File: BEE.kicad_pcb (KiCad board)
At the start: 2 copper layers, 74 x 38 mm, 32 parts, among them J1 RPI1_header, J10 Conn_01x02, J11 Conn_01x02, J12 Conn_01x02, J15 Conn_01x09, J2 Conn_02x05_Odd_Even, J3 Conn_02x03_Odd_Even, J4 Conn_01x06, J5 Conn_02x10_Odd_Even, J6 Conn_01x08, J7 Conn_01x03, J8 Conn_01x08, J9 Conn_01x02, SW1 SW_Push, SW2 SW_Push, SW3 SW_Push, U1 MCP3008, U2 MCP4911

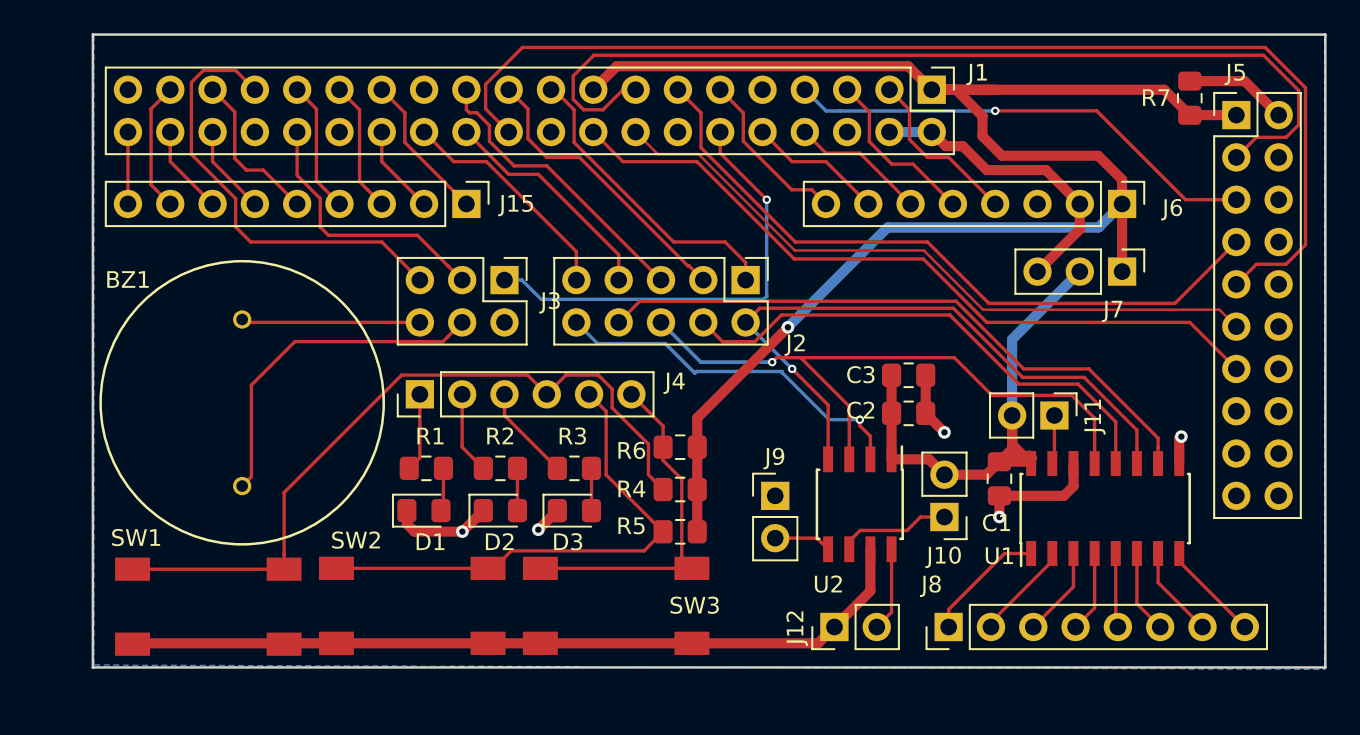
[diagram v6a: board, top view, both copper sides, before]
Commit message: wip: with mounting holes, board a little bit bigger
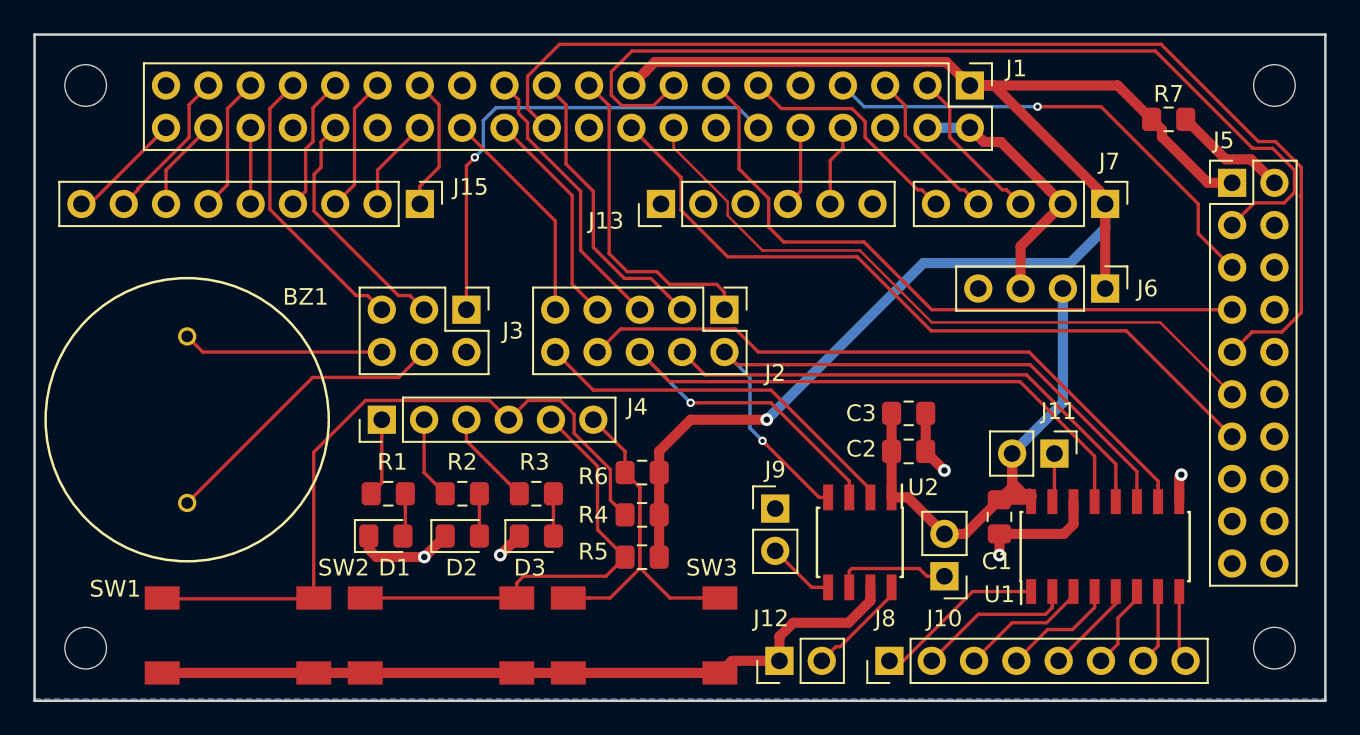
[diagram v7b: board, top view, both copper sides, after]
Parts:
- added H1: MountingHole, MountingHole:MountingHole_2.5mm, F.Cu at (99.6, 83.1)
- added H2: MountingHole, MountingHole:MountingHole_2.5mm, F.Cu at (99.6, 116.8)
- added H3: MountingHole, MountingHole:MountingHole_2.5mm, F.Cu at (170.9, 83.1)
- added H4: MountingHole, MountingHole:MountingHole_2.5mm, F.Cu at (170.9, 116.8)
- added J13: Conn_01x06, Connector_PinHeader_2.54mm:PinHeader_1x06_P2.54mm_Vertical, F.Cu at (134.1, 90.2)
- J6: value Conn_01x08 -> Conn_01x04; footprint Connector_PinHeader_2.54mm:PinHeader_1x08_P2.54mm_Vertical -> Connector_PinHeader_2.54mm:PinHeader_1x04_P2.54mm_Vertical
- J7: value Conn_01x03 -> Conn_01x05; footprint Connector_PinHeader_2.54mm:PinHeader_1x03_P2.54mm_Vertical -> Connector_PinHeader_2.54mm:PinHeader_1x05_P2.54mm_Vertical
- moved J6 5.18 mm to (160.8, 95.2)
- moved J7 4.19 mm to (160.8, 90.2)
- moved J8 4.10 mm to (147.8, 117.6)
- moved J5 4.07 mm to (168.4, 88.9)
- moved J12 3.88 mm to (141.2, 117.6)
- moved J10 3.56 mm to (151.1, 112.5)
- moved BZ1 3.45 mm to (105.7, 103.1)
- moved J3 2.90 mm to (122.4, 96.5)
- moved J15 2.79 mm to (119.6, 90.2)
- moved D1 2.75 mm to (117.6, 110.1)
- moved J4 2.75 mm to (117.3, 103.1)
- moved R1 2.75 mm to (117.7, 107.6)
- moved R4 2.75 mm to (133.0, 108.8)
- moved R5 2.75 mm to (133.0, 111.4)
- moved R6 2.75 mm to (133.0, 106.3)
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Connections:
- J15 pad 5: /BCM19 -> /BCM16
- J15 pad 6: /BCM16 -> /BCM19
- J5 pad 15: Net-(J5-Pad15) -> (no net)
- J5 pad 17: Net-(J5-Pad17) -> (no net)
- J5 pad 19: Net-(J5-Pad19) -> (no net)
- J6 pad 2: +5V -> VDD
- J6 pad 3: GND -> +5V
- J6 pad 4: /BCM2_SDA -> GND
- J7 pad 2: VDD -> +5V
- J7 pad 3: +5V -> /BCM2_SDA
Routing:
- net /SCLK: track 38.7 -> 49.4 mm
- net /BCM13_PWM1: track 26.7 -> 17.2 mm
- net +3V3: track 102.0 -> 96.5 mm
- net /SW1: track 21.1 -> 25.5 mm
- net /BCM17: track 10.2 -> 14.2 mm
- net Net-(J8-Pad2): track 6.89 -> 10.5 mm
- net /SW2: track 30.6 -> 27.2 mm
- net /BCM14_TX: track 8.14 -> 4.89 mm
- net /BCM15_RX: track 8.14 -> 4.89 mm
- net Net-(J8-Pad1): track 8.35 -> 11.2 mm
- net /BCM21: track 4.32 -> 6.97 mm
- net Net-(BZ1-Pad1): track 20.5 -> 18.0 mm
- net Net-(J8-Pad3): track 6.04 -> 8.47 mm
- net +5V: track 18.3 -> 16.2 mm
- net Net-(J8-Pad4): track 5.34 -> 7.43 mm
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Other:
- board size 74 x 38 mm -> 77.5 x 40 mm

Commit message: uart connector with jumpers to select crossed or direct connection. rerouted and labeled
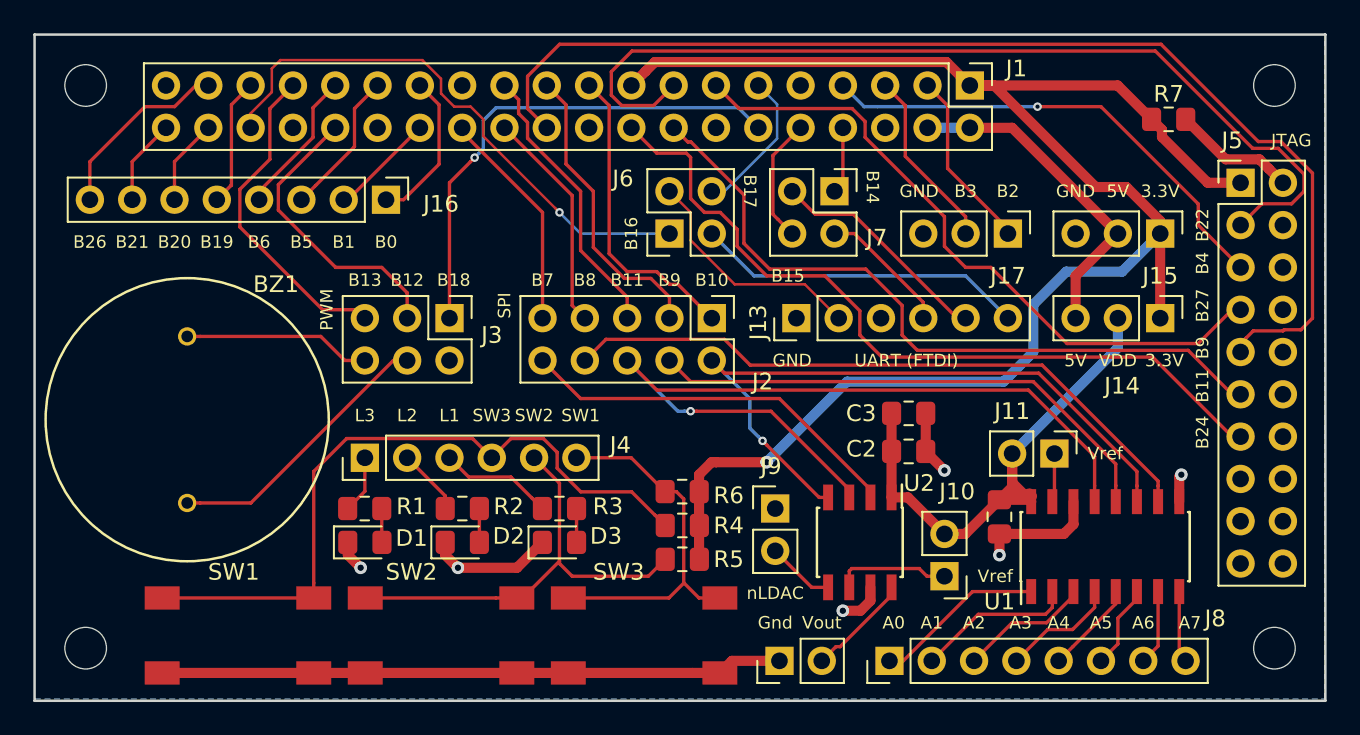
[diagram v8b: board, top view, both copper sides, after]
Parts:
- added J14: Conn_01x03, Connector_PinHeader_2.54mm:PinHeader_1x03_P2.54mm_Vertical, F.Cu at (164.1, 97.0)
- added J16: Conn_01x08, Connector_PinHeader_2.54mm:PinHeader_1x08_P2.54mm_Vertical, F.Cu at (117.6, 89.9)
- added J17: Conn_01x03, Connector_PinHeader_2.54mm:PinHeader_1x03_P2.54mm_Vertical, F.Cu at (154.9, 91.9)
- J15: value Conn_01x09 -> Conn_01x03; footprint Connector_PinHeader_2.54mm:PinHeader_1x09_P2.54mm_Vertical -> Connector_PinHeader_2.54mm:PinHeader_1x03_P2.54mm_Vertical
- J6: value Conn_01x04 -> Conn_02x02_Odd_Even; footprint Connector_PinHeader_2.54mm:PinHeader_1x04_P2.54mm_Vertical -> Connector_PinHeader_2.54mm:PinHeader_2x02_P2.54mm_Vertical
- J7: value Conn_01x05 -> Conn_02x02_Odd_Even; footprint Connector_PinHeader_2.54mm:PinHeader_1x05_P2.54mm_Vertical -> Connector_PinHeader_2.54mm:PinHeader_2x02_P2.54mm_Vertical
- moved J15 44.5 mm to (164.1, 91.9)
- moved J6 26.4 mm to (134.6, 91.9), turned to 90 degrees
- moved J7 16.3 mm to (144.5, 89.4)
- moved J13 10.6 mm to (142.2, 97.0)
- moved R6 2.66 mm to (135.4, 107.4)
- moved J4 2.50 mm to (116.3, 105.4)
- moved R4 2.50 mm to (135.4, 109.5)
- moved R5 2.42 mm to (135.4, 111.5)
- moved R1 1.67 mm to (116.3, 108.5)
- moved R3 1.65 mm to (128.0, 108.5)
- moved D3 1.44 mm to (128.0, 110.5)
- moved D1 1.32 mm to (116.3, 110.5)
- moved J3 1.14 mm to (121.4, 97.0)
- moved J2 0.92 mm to (137.2, 97.0)
- moved R2 0.89 mm to (122.2, 108.5)
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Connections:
- J1 pad 11: /BCM17 -> /BCM17_RTS1
- J1 pad 36: /BCM16 -> /BCM16_CTS1
- J13 pad 2: (no net) -> Net-(J13-Pad2)
- J13 pad 4: /BCM15_RX -> Net-(J13-Pad4)
- J13 pad 5: /BCM14_TX -> Net-(J13-Pad5)
- J13 pad 6: (no net) -> Net-(J13-Pad6)
- J15 pad 1: /BCM0 -> +3V3
- J15 pad 2: /BCM1 -> +5V
- J15 pad 3: /BCM5 -> GND
- J6 pad 1: +3V3 -> /BCM16_CTS1
- J6 pad 2: VDD -> Net-(J13-Pad2)
- J6 pad 3: +5V -> Net-(J13-Pad6)
- J6 pad 4: GND -> /BCM17_RTS1
- J7 pad 1: +3V3 -> /BCM14_TX
- J7 pad 2: +5V -> Net-(J13-Pad4)
- J7 pad 3: /BCM2_SDA -> Net-(J13-Pad5)
- J7 pad 4: /BCM3_SCL -> /BCM15_RX
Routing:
- net /BCM16_CTS1: track 0.00 -> 33.6 mm, vias 0 -> 1
- net Net-(J13-Pad6): track 0.00 -> 19.9 mm
- net Net-(J13-Pad2): track 0.00 -> 14.3 mm
- net /BCM17: track 14.2 -> 0.00 mm
- net Net-(J13-Pad5): track 0.00 -> 13.6 mm
- net /BCM17_RTS1: track 0.00 -> 8.89 mm
- net Net-(J13-Pad4): track 0.00 -> 8.50 mm
- net +3V3: track 96.5 -> 101.6 mm
- net /BCM16: track 4.57 -> 0.00 mm
- net GND: track 66.7 -> 62.4 mm, vias 5 -> 6
- net +5V: track 16.2 -> 20.2 mm
- net /SW1: track 25.5 -> 22.4 mm
- net /BCM12_PWM0: track 14.6 -> 17.7 mm
- net /BCM15_RX: track 4.89 -> 7.52 mm
- net /BCM13_PWM1: track 17.2 -> 19.6 mm
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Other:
- board text added: "3.3V"
- board text added: "5V"
- board text added: "A0"
- board text added: "A1"
- board text added: "A2"
- board text added: "A3"
- board text added: "A4"
- board text added: "A5"
- board text added: "A6"
- board text added: "A7"
- board text added: "B0"
- board text added: "B1"
- board text added: "B10"
- board text added: "B11"
- board text added: "B12"
- board text added: "B13"
- board text added: "B14"
- board text added: "B15"
- board text added: "B16"
- board text added: "B17"
- board text added: "B18"
- board text added: "B19"
- board text added: "B2"
- board text added: "B20"
- board text added: "B21"
- board text added: "B22"
- board text added: "B24"
- board text added: "B26"
- board text added: "B27"
- board text added: "B3"
- board text added: "B4"
- board text added: "B5"
- board text added: "B6"
- board text added: "B7"
- board text added: "B8"
- board text added: "B9"
- board text added: "GND"
- board text added: "Gnd"
- board text added: "JTAG"
- board text added: "L1"
- board text added: "L2"
- board text added: "L3"
- board text added: "PWM"
- board text added: "SPI"
- board text added: "SW1"
- board text added: "SW2"
- board text added: "SW3"
- board text added: "UART (FTDI)"
- board text added: "VDD"
- board text added: "Vout"
- board text added: "Vref"
- board text added: "nLDAC"
